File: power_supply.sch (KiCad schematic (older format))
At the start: 17 parts, among them U3 AZ1117, U4 LMR16006X, U5 AP2210-3.3

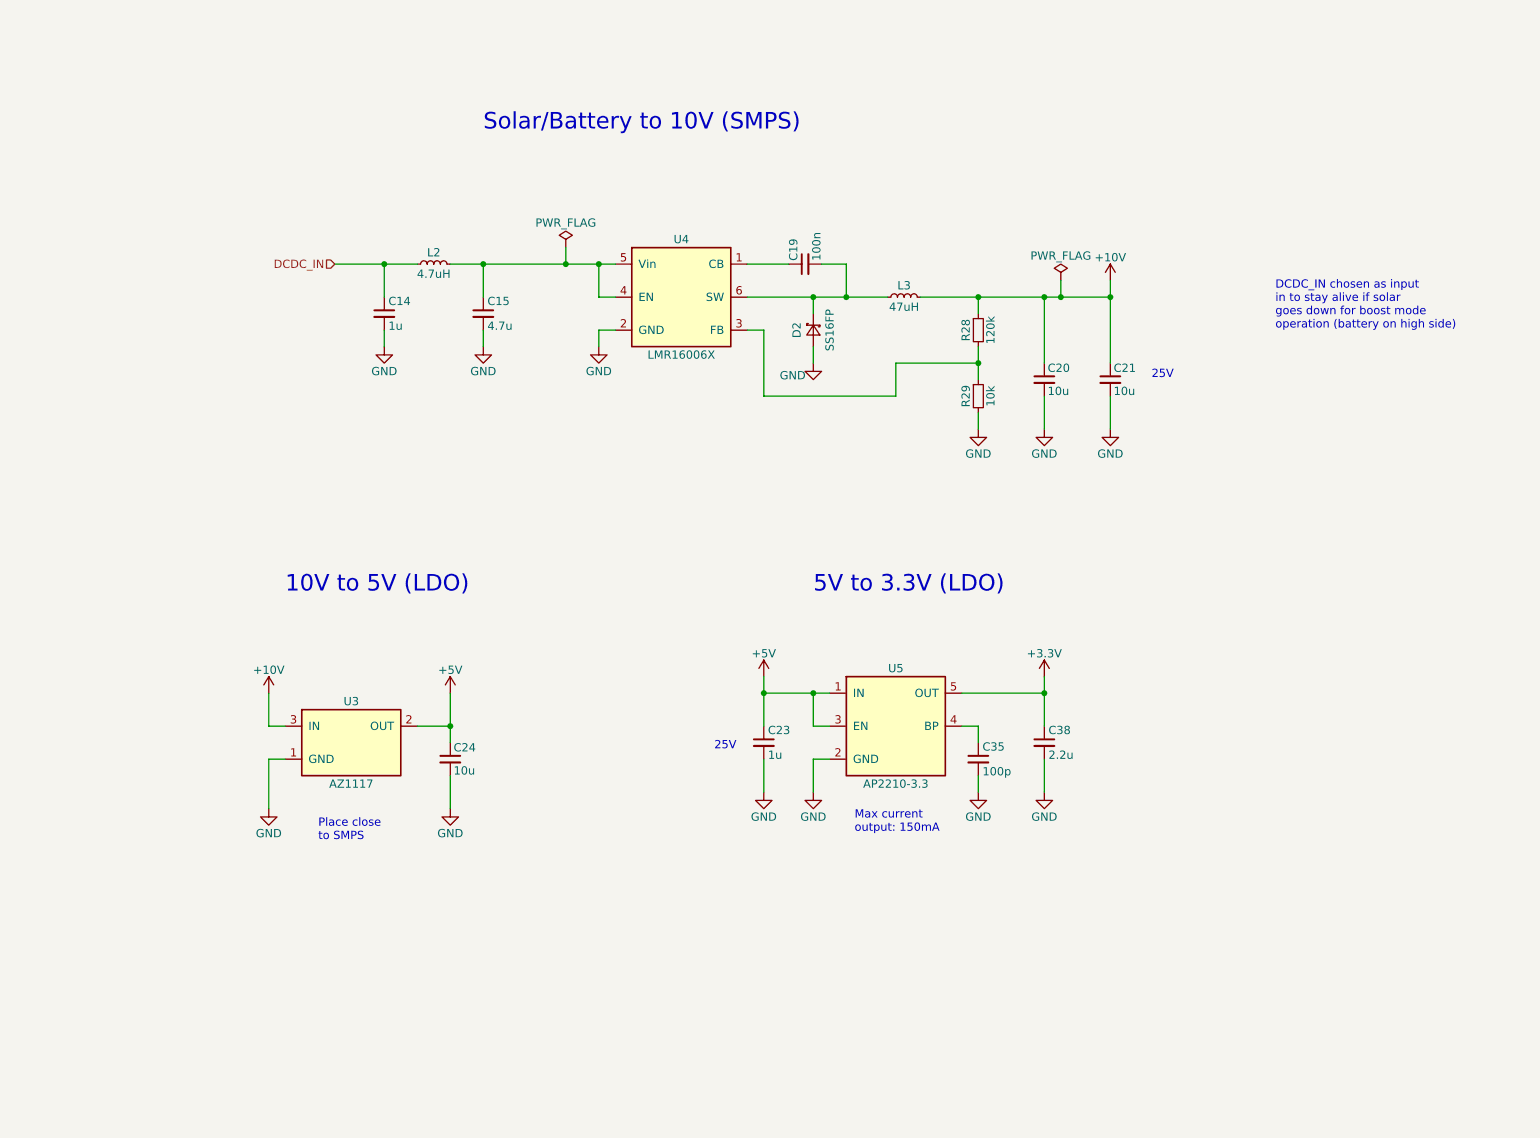
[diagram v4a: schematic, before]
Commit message: Revision 0.9 for first small production batch - Switchable power supply for bus and UEXT (to be make sure to reach very low power consumption during LVD conditions) - MLCCs for EMC added to each high power input/output - Re-arrangement of some connectors after initial tests with housing
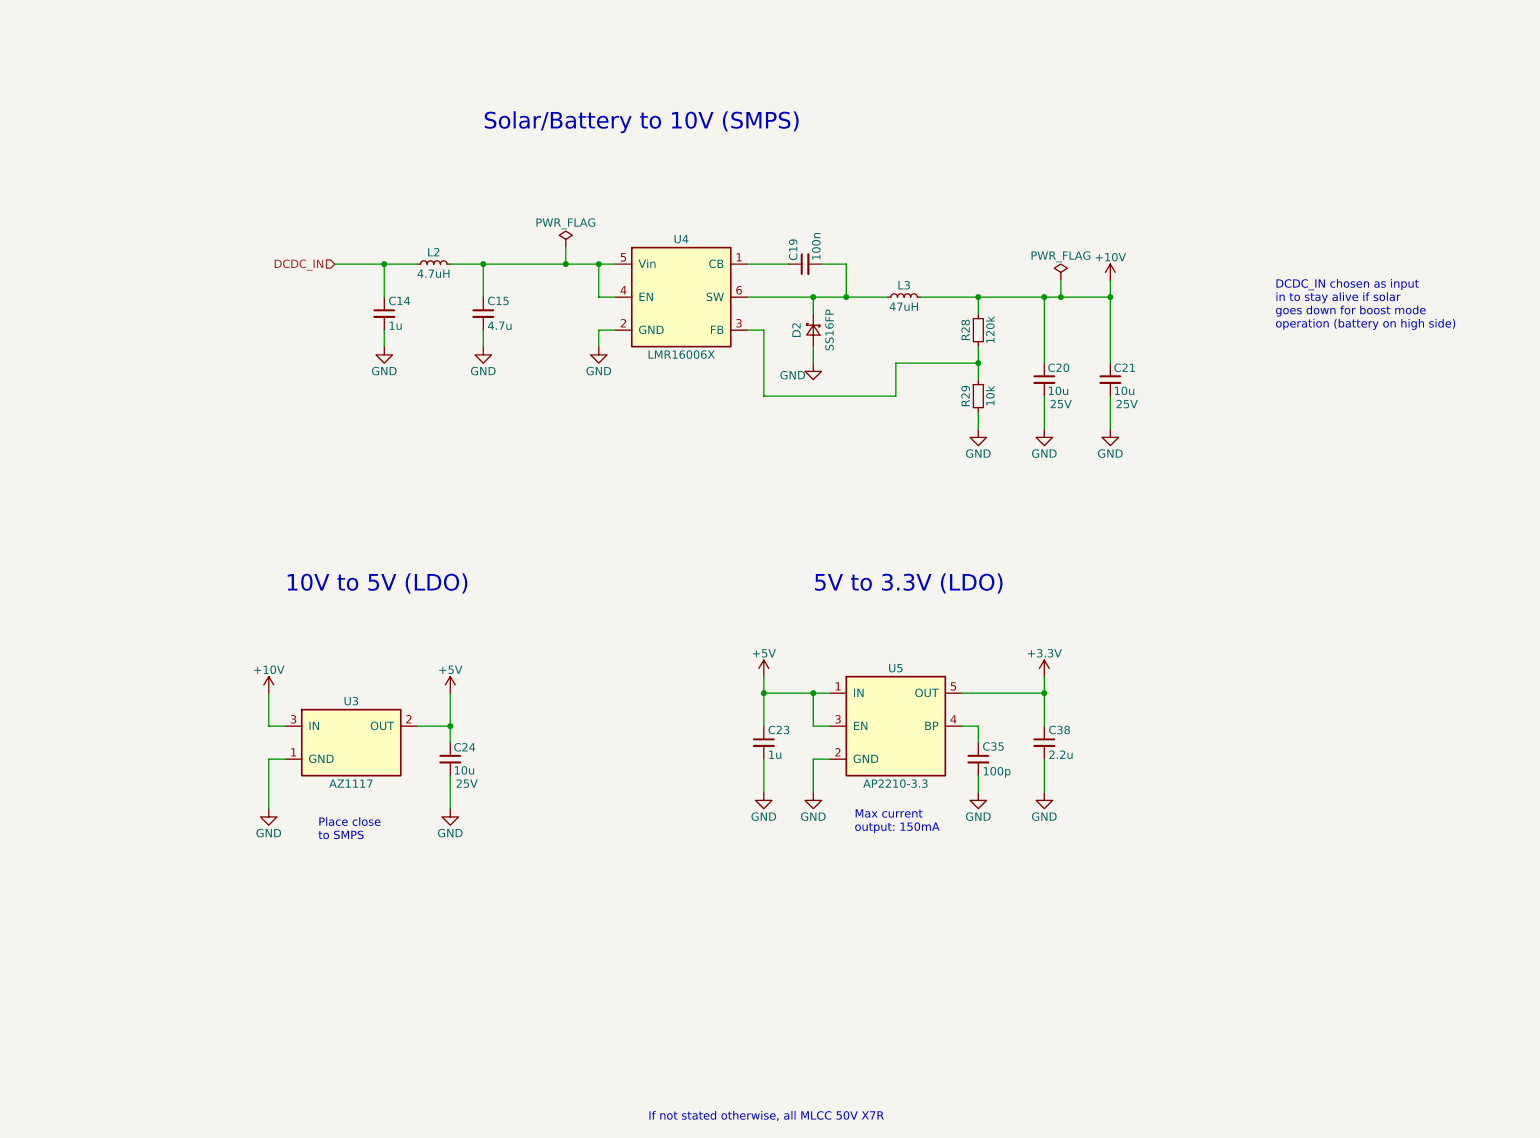
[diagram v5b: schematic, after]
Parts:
- C20, C21, C24: Remarks (none) -> 25V
- C23: footprint LibreSolar:C_0603_1608 -> LibreSolar:C_0805_2012; PartNumber GRM188R61E105KA12D -> GRJ21BR71H105KE01; Remarks 25V, X5R -> (none)
- R29: PartNumber RC0603FR-07150KL -> RC0603FR-0710KL
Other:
- note added: "If not stated otherwise, all MLCC 50V X7R"
- note removed: "25V"
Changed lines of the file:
@@
 Sheet 4 6
 Title "MPPT Charger 20A"
-Date "2017-08-06"
-Rev "0.8"
+Date "2017-12-11"
+Rev "0.9"
 Comp "Libre Solar"
 Comment1 "Author: Martin Jäger"
@@
 F 3 "" H 7100 3200 50  0000 C CNN
 F 4 "Yageo" H 1400 200 50  0001 C CNN "Manufacturer"
-F 5 "RC0603FR-07150KL" H 1400 200 50  0001 C CNN "PartNumber"
-F 6 "" H 1400 200 50  0001 C CNN "SPR"
-F 7 "" H 1400 200 50  0001 C CNN "SPN"
-F 8 "" H 1400 200 50  0001 C CNN "SPURL"
+F 5 "RC0603FR-0710KL" H 1400 200 50  0001 C CNN "PartNumber"
 	1    7100 3200
 	1    0    0    -1
@@
 F 0 "C23" H 5825 5375 50  0000 L CNN
 F 1 "1u" H 5825 5225 50  0000 L CNN
-F 2 "LibreSolar:C_0603_1608" H 5800 5100 50  0001 C CNN
+F 2 "LibreSolar:C_0805_2012" H 5800 5100 50  0001 C CNN
 F 3 "" H 5825 5375 50  0000 C CNN
 F 4 "Murata" H -2200 2550 50  0001 C CNN "Manufacturer"
-F 5 "GRM188R61E105KA12D" H -2200 2550 50  0001 C CNN "PartNumber"
-F 6 "" H -2200 2550 50  0001 C CNN "SPR"
-F 7 "" H -2200 2550 50  0001 C CNN "SPN"
-F 8 "" H -2200 2550 50  0001 C CNN "SPURL"
-F 9 "25V, X5R" H 0   0   60  0001 C CNN "Remarks"
-F 10 "" H 0   0   60  0001 C CNN "Comment"
+F 5 "GRJ21BR71H105KE01" H -2200 2550 50  0001 C CNN "PartNumber"
+F 6 "" H 0   0   60  0001 C CNN "Remarks"
 	1    5800 5300
 	1    0    0    -1
@@
 F 4 "Murata" H 1400 250 50  0001 C CNN "Manufacturer"
 F 5 "GRM21BR61E106KA73L" H 1400 250 50  0001 C CNN "PartNumber"
-F 6 "" H 1400 250 50  0001 C CNN "SPR"
-F 7 "" H 1400 250 50  0001 C CNN "SPN"
-F 8 "" H 1400 250 50  0001 C CNN "SPURL"
+F 6 "25V" H 8000 2950 50  0000 C CNN "Remarks"
 	1    7900 3100
 	1    0    0    -1
@@
 F 4 "Murata" H 1400 250 50  0001 C CNN "Manufacturer"
 F 5 "GRM21BR61E106KA73L" H 1400 250 50  0001 C CNN "PartNumber"
-F 6 "" H 1400 250 50  0001 C CNN "SPR"
-F 7 "" H 1400 250 50  0001 C CNN "SPN"
-F 8 "" H 1400 250 50  0001 C CNN "SPURL"
+F 6 "25V" H 7600 2950 50  0000 C CNN "Remarks"
 	1    7500 3100
 	1    0    0    -1
@@
 F 4 "Murata" H 1400 200 50  0001 C CNN "Manufacturer"
 F 5 "GRM188R71H104KA93D" H 1400 200 50  0001 C CNN "PartNumber"
-F 6 "" H 1400 200 50  0001 C CNN "SPR"
-F 7 "" H 1400 200 50  0001 C CNN "SPN"
-F 8 "" H 1400 200 50  0001 C CNN "SPURL"
 	1    6050 2400
 	0    -1   -1   0
@@
 F 4 "Murata" H 1100 -50 50  0001 C CNN "Manufacturer"
 F 5 "GRJ21BC72A105KE11L" H 1100 -50 50  0001 C CNN "PartNumber"
-F 6 "" H 1100 -50 50  0001 C CNN "SPR"
-F 7 "" H 1100 -50 50  0001 C CNN "SPN"
-F 8 "" H 1100 -50 50  0001 C CNN "SPURL"
-F 9 "" H 0   0   60  0001 C CNN "Comment"
-F 10 "100V, X7S" H 0   0   60  0001 C CNN "Remarks"
+F 6 "100V, X7S" H 0   0   60  0001 C CNN "Remarks"
 	1    3500 2700
 	1    0    0    -1
@@
 F 4 "Murata" H -2250 2600 50  0001 C CNN "Manufacturer"
 F 5 "GRM1885C2A101JA01D" H -2250 2600 50  0001 C CNN "PartNumber"
-F 6 "" H -2250 2600 50  0001 C CNN "SPR"
-F 7 "" H -2250 2600 50  0001 C CNN "SPN"
-F 8 "" H -2250 2600 50  0001 C CNN "SPURL"
 	1    7100 5400
 	1    0    0    -1
@@
 F 4 "Murata" H -2250 2500 50  0001 C CNN "Manufacturer"
 F 5 "GRM188R60J225KE19D" H -2250 2500 50  0001 C CNN "PartNumber"
-F 6 "" H -2250 2500 50  0001 C CNN "SPR"
-F 7 "" H -2250 2500 50  0001 C CNN "SPN"
-F 8 "" H -2250 2500 50  0001 C CNN "SPURL"
-F 9 "" H 0   0   60  0001 C CNN "Comment"
-F 10 "6.3V, X5R" H 0   0   60  0001 C CNN "Remarks"
+F 6 "6.3V, X5R" H 0   0   60  0001 C CNN "Remarks"
 	1    7500 5300
 	1    0    0    -1
@@
 Text Notes 6350 5850 0    50   ~ 0
 Max current \noutput: 150mA
-Text Notes 5500 5350 0    50   ~ 0
-25V
-Text Notes 8150 3100 0    50   ~ 0
-25V
 Text HLabel 3200 2400 0    50   Input ~ 0
 DCDC_IN
@@
 F 4 "Murata" H -2600 2550 50  0001 C CNN "Manufacturer"
 F 5 "GRM21BR61E106KA73L" H -2600 2550 50  0001 C CNN "PartNumber"
+F 6 "25V" H 4000 5250 50  0000 C CNN "Remarks"
 	1    3900 5400
 	1    0    0    -1
@@
 	1    0    0    -1
 $EndComp
+Text Notes 5100 7600 0    50   ~ 0
+If not stated otherwise, all MLCC 50V X7R
 $EndSCHEMATC

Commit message: Final version for Jan/2018 production
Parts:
- C23: value 1u -> 2.2u; footprint LibreSolar:C_0805_2012 -> LibreSolar:C_0603_1608; PartNumber GRJ21BR71H105KE01 -> GRM188R61E225KA12D; Remarks (none) -> 25V, X5R
- C38: PartNumber GRM188R60J225KE19D -> GRM188R61E225KA12D; Remarks 6.3V, X5R -> 25V, X5R
- U4: PartNumber LMR16006X -> LMR16006XDDCR
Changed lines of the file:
@@
 Sheet 4 6
 Title "MPPT Charger 20A"
-Date "2017-12-11"
-Rev "0.9"
+Date "2018-01-18"
+Rev "0.10"
 Comp "Libre Solar"
 Comment1 "Author: Martin Jäger"
@@
 P 5800 5300
 F 0 "C23" H 5825 5375 50  0000 L CNN
-F 1 "1u" H 5825 5225 50  0000 L CNN
-F 2 "LibreSolar:C_0805_2012" H 5800 5100 50  0001 C CNN
+F 1 "2.2u" H 5825 5225 50  0000 L CNN
+F 2 "LibreSolar:C_0603_1608" H 5800 5100 50  0001 C CNN
 F 3 "" H 5825 5375 50  0000 C CNN
 F 4 "Murata" H -2200 2550 50  0001 C CNN "Manufacturer"
-F 5 "GRJ21BR71H105KE01" H -2200 2550 50  0001 C CNN "PartNumber"
-F 6 "" H 0   0   60  0001 C CNN "Remarks"
+F 5 "GRM188R61E225KA12D" H -2200 2550 50  0001 C CNN "PartNumber"
+F 6 "25V, X5R" H 0   0   60  0001 C CNN "Remarks"
 	1    5800 5300
 	1    0    0    -1
@@
 F 3 "" H 7525 5375 50  0000 C CNN
 F 4 "Murata" H -2250 2500 50  0001 C CNN "Manufacturer"
-F 5 "GRM188R60J225KE19D" H -2250 2500 50  0001 C CNN "PartNumber"
-F 6 "6.3V, X5R" H 0   0   60  0001 C CNN "Remarks"
+F 5 "GRM188R61E225KA12D" H -2250 2500 50  0001 C CNN "PartNumber"
+F 6 "25V, X5R" H 0   0   60  0001 C CNN "Remarks"
 	1    7500 5300
 	1    0    0    -1
@@
 F 3 "" H 4900 3000 50  0000 C CNN
 F 4 "Texas Instruments" H 1400 250 50  0001 C CNN "Manufacturer"
-F 5 "LMR16006X" H 1400 250 50  0001 C CNN "PartNumber"
+F 5 "LMR16006XDDCR" H 1400 250 50  0001 C CNN "PartNumber"
 	1    5300 2600
 	1    0    0    -1

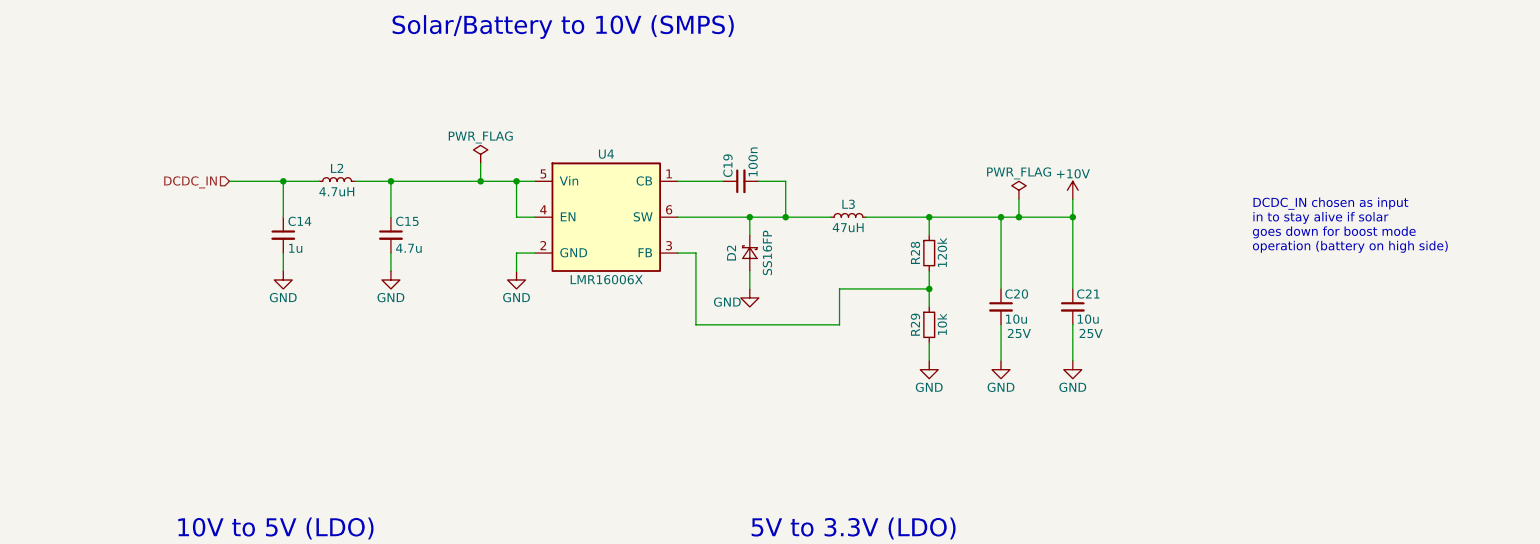
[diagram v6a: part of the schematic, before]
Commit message: Adjustments to use MP2459 as SMPS (previous one out of stock)
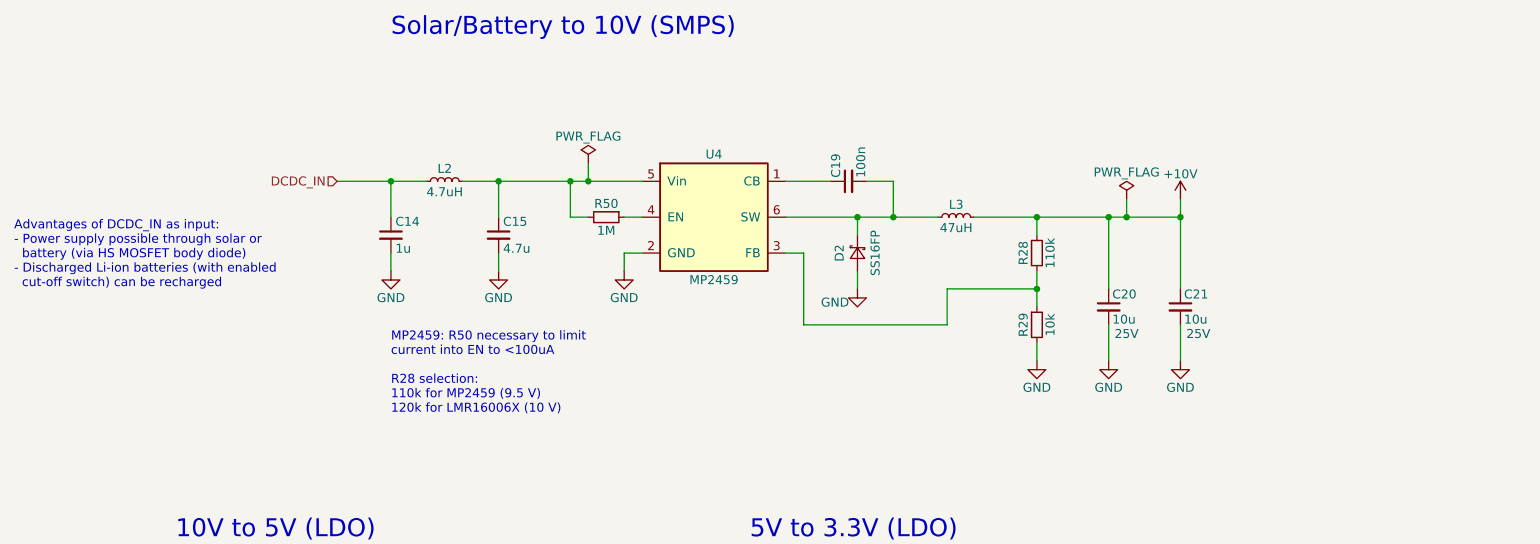
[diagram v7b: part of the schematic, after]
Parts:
- added R50: 1M, LibreSolar:R_0603_1608, symbol device:R_Small
- L3: footprint LibreSolar:L_Wuerth_WE-TPC-58xx -> LibreSolar:Bourns_SRN6045TA; Alternative WE-TPC-5828 744053470 -> Tayo Yuden NR6045T470M; PartNumber SRR5028-470Y -> SRR6045TA-470Y
- R28: value 120k -> 110k; PartNumber RC0603FR-07120KL -> RC0603FR-07110KL
- U4: value LMR16006X -> MP2459; Alternative (none) -> LMR16006XDDCR; Manufacturer Texas Instruments -> Monolithic Power; PartNumber LMR16006XDDCR -> MP2459
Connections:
- net at C15.1, L2.2, U4.5 (Vin): now also R50.2; no longer U4.4 (EN)
- new net: R50.1, U4.4 (EN)
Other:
- note added: "Advantages of DCDC_IN as input:\n- Power supply possible through solar or\n battery (via HS MOSFET body diode)\n- Discharged Li-ion batteries (with enabled\n cut-off switch) can be recharged"
- note added: "MP2459: R50 necessary to limit\ncurrent into EN to <100uA \n\nR28 selection:\n110k for MP2459 (9.5 V)\n120k for LMR16006X (10 V)"
- note removed: "DCDC_IN chosen as input\nin to stay alive if solar\ngoes down for boost mode\noperation (battery on high side)"
- moved on the sheet: C14, C15, C19, C20, C21, D2, L2, L3, R28, R29, U4

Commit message: Power supply inductor changed to Tayo Yuden
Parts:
- L3: Alternative Tayo Yuden NR6045T470M -> Bourns SRR6045TA-470Y; Manufacturer Bourns -> Tayo Yuden; PartNumber SRR6045TA-470Y -> NR6045T470M
- U4: PartNumber MP2459 -> MP2459GJ-Z
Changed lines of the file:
@@
 F 2 "LibreSolar:Bourns_SRN6045TA" V 7250 2600 50  0001 C CNN
 F 3 "" V 7250 2600 50  0000 C CNN
-F 4 "Bourns" H 7250 2600 60  0001 C CNN "Manufacturer"
-F 5 "SRR6045TA-470Y" H 7250 2600 60  0001 C CNN "PartNumber"
-F 6 "Tayo Yuden NR6045T470M" H 7250 2600 60  0001 C CNN "Alternative"
+F 4 "Tayo Yuden" H 7250 2600 60  0001 C CNN "Manufacturer"
+F 5 "NR6045T470M" H 7250 2600 60  0001 C CNN "PartNumber"
+F 6 "Bourns SRR6045TA-470Y" H 7250 2600 60  0001 C CNN "Alternative"
 	1    7250 2600
 	0    -1   -1   0
@@
 F 3 "" H 5500 3000 50  0000 C CNN
 F 4 "Monolithic Power" H 2000 250 50  0001 C CNN "Manufacturer"
-F 5 "MP2459" H 2000 250 50  0001 C CNN "PartNumber"
+F 5 "MP2459GJ-Z" H 2000 250 50  0001 C CNN "PartNumber"
 F 6 "LMR16006XDDCR" H 5900 2600 60  0001 C CNN "Alternative"
 	1    5900 2600
